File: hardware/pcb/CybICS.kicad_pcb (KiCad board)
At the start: 2 copper layers, 160 x 100 mm, 79 parts, among them J1 Raspberry_Pi_2_3, J2 Conn_01x03_Pin, J3 Conn_01x05_Pin, J4 USB_C_Receptacle_USB2.0, SW1 SW_Push, SW2 SW_Push, SW3 SW_Push, U1 STM32G070RBTx

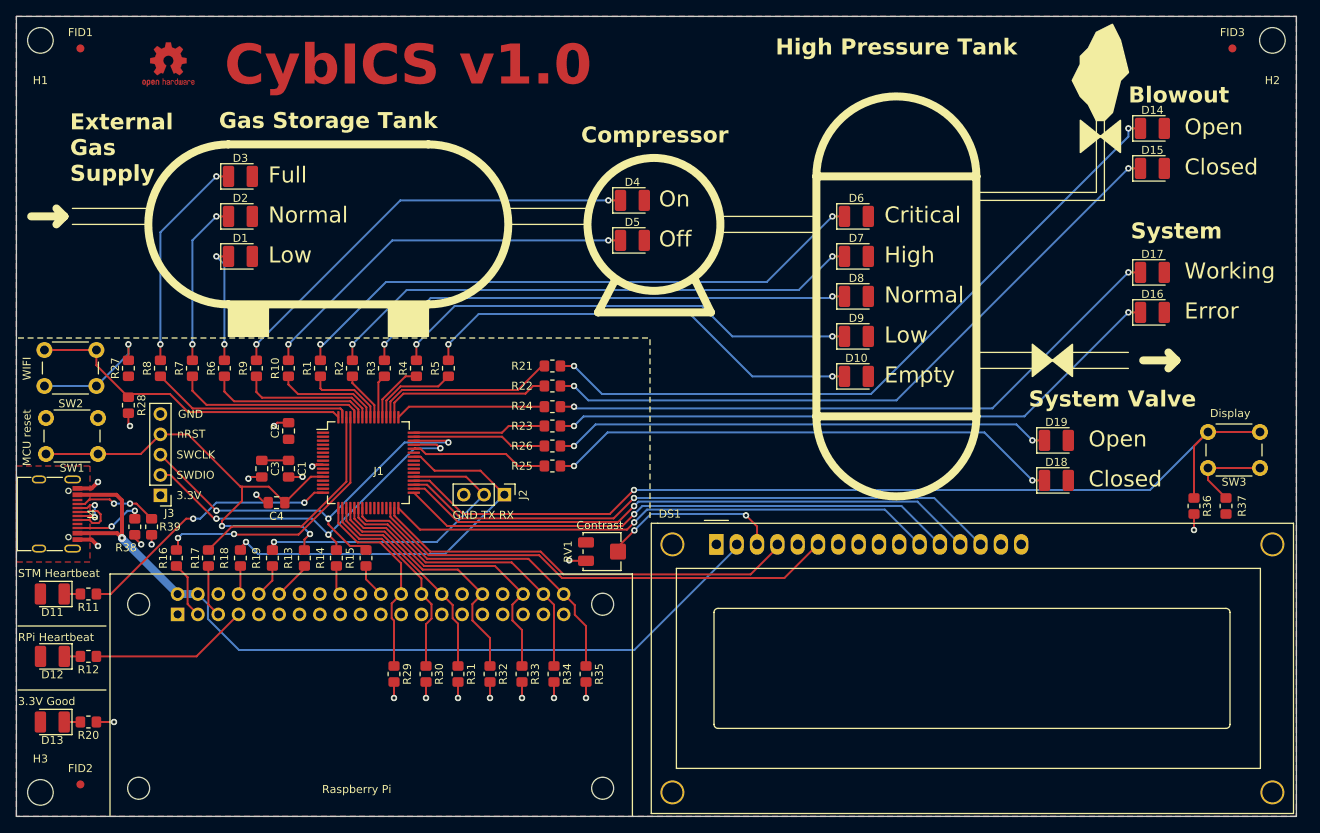
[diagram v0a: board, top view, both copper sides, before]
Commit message: feat(hardware)!: hardware v1.1 upgrade, KiCad 10 and JLCPCB fixes (#240)
* fix(hardware): exclude fiducials from the JLCPCB position files

FID1-FID3 carried exclude_from_bom but not exclude_from_pos_files,
unlike the mounting holes and the OSHW logo, which set both. The
fiducials therefore reached the CPL while being absent from the BOM,
and JLCPCB rejected the assembly quote with "FID1,FID2,FID3
designators don't exist in the BOM file" (reported in #238). Fiducials
are alignment marks rather than parts, so the dialog was harmless, but
every person ordering this board had to decide that for themselves.

Verified with kicad-cli 8.0.9: pcb export pos --smd-only drops from 69
to 66 rows against the previous board, the three removed designators
are exactly FID1, FID2 and FID3, and ERC and DRC still report 0
violations and 0 unconnected items. Claude has no access to the
hardware, so the JLCPCB upload itself is unverified.

Refs #238

Co-Authored-By: Claude Opus 5 (1M context) <noreply@anthropic.com>
Claude-Session: https://claude.ai/code/session_011zbigHZaGiZii3etPu8DwT

* fix(hardware): correct the LED series resistors and the yellow LED part

R1/R2/R4/R6/R10/R21/R23/R25 are drawn as 330R but carried C52548, which
is 0805W8F330LT5E -- 330 mΩ, not 330 Ω. The L in that part code is
Uniroyal's milliohm marker, and both LCSC and JLCPCB's parts database
index it at 0.33 Ω. The six red, two yellow and two blue indicators
were therefore assembled with no effective current limiting: each one
settles at roughly its full rated current against the GPIO's own
impedance, and ten such pins take the STM32G070 past its 100 mA total
I/O budget. Corrected to C17630 (0805W8F3300T5E, 330 Ω), which is also
a basic-library part.

That correction alone would have regressed two colours, because the
0.33 Ω part was the only reason they lit at all:

  - D7/D9 are drawn as LED YELLOW but carried C434441, SZYY1206W -- a
    *white* LED with a yellow lens and Vf 3.1 V. Across a real 330 Ω
    fro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
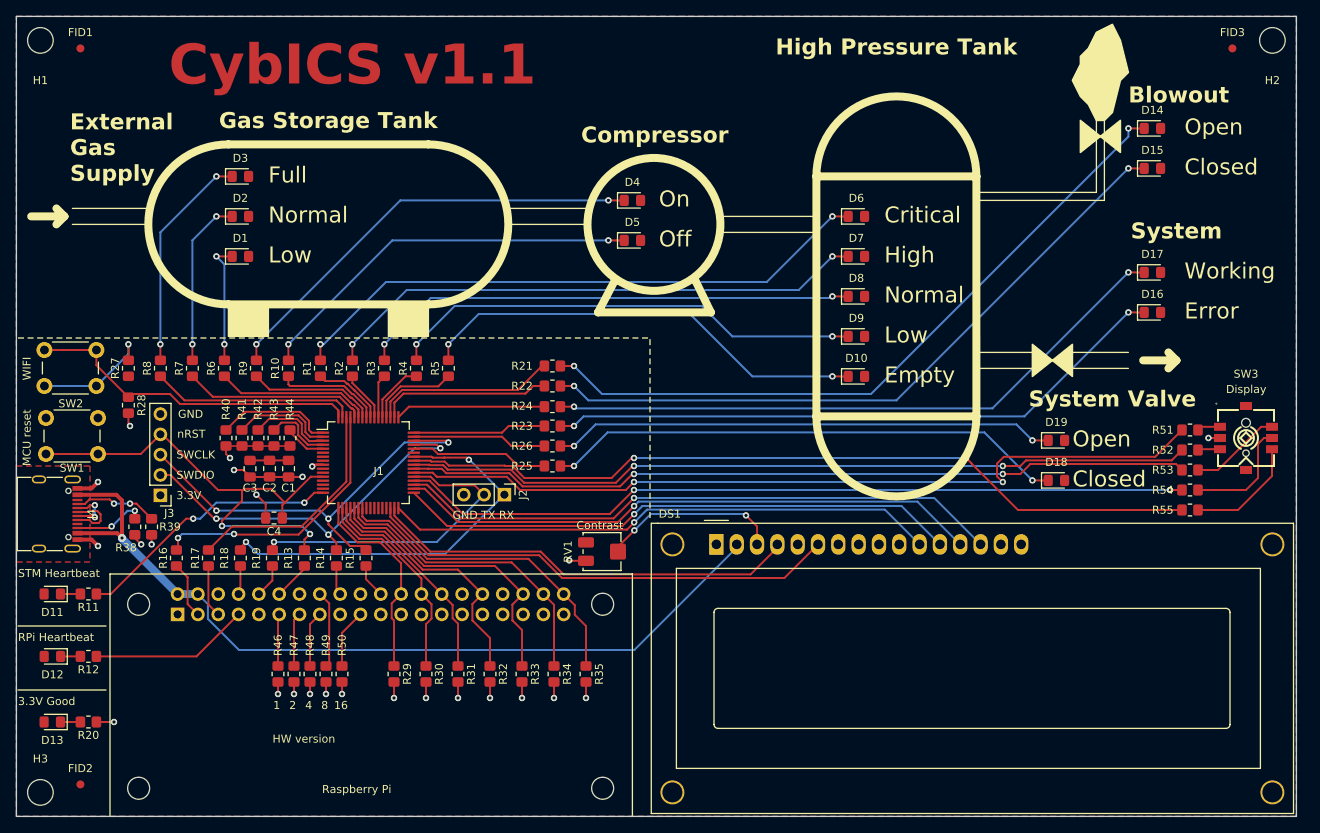
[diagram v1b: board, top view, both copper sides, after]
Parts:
- removed #SYM1: OSHW-Logo2_7.3x6mm_Copper, Symbol:OSHW-Logo2_7.3x6mm_Copper
- removed R36: 10kR, Resistor_SMD:R_0805_2012Metric_Pad1.20x1.40mm_HandSolder
- removed R37: 1kR, Resistor_SMD:R_0805_2012Metric_Pad1.20x1.40mm_HandSolder
- added R40: 1kR, Resistor_SMD:R_0805_2012Metric_Pad1.20x1.40mm_HandSolder, F.Cu at (77.0, 103.5)
- added R41: 1kR, Resistor_SMD:R_0805_2012Metric_Pad1.20x1.40mm_HandSolder, F.Cu at (79.0, 103.5)
- added R42: 1kR, Resistor_SMD:R_0805_2012Metric_Pad1.20x1.40mm_HandSolder, F.Cu at (81.0, 103.5)
- added R43: 1kR, Resistor_SMD:R_0805_2012Metric_Pad1.20x1.40mm_HandSolder, F.Cu at (83.0, 103.5)
- added R44: 1kR, Resistor_SMD:R_0805_2012Metric_Pad1.20x1.40mm_HandSolder, F.Cu at (85.0, 103.5)
- added R46: 1kR, Resistor_SMD:R_0805_2012Metric_Pad1.20x1.40mm_HandSolder, F.Cu at (83.5, 133.0)
- added R47: 1kR, Resistor_SMD:R_0805_2012Metric_Pad1.20x1.40mm_HandSolder, F.Cu at (85.5, 133.0)
- added R48: 1kR, Resistor_SMD:R_0805_2012Metric_Pad1.20x1.40mm_HandSolder, F.Cu at (87.5, 133.0)
- added R49: 1kR, Resistor_SMD:R_0805_2012Metric_Pad1.20x1.40mm_HandSolder, F.Cu at (89.5, 133.0)
- added R50: 1kR, Resistor_SMD:R_0805_2012Metric_Pad1.20x1.40mm_HandSolder, F.Cu at (91.5, 133.0)
- added R51: 1kR, Resistor_SMD:R_0805_2012Metric_Pad1.20x1.40mm_HandSolder, F.Cu at (197.5, 102.5)
- added R52: 1kR, Resistor_SMD:R_0805_2012Metric_Pad1.20x1.40mm_HandSolder, F.Cu at (197.5, 105.0)
- added R53: 1kR, Resistor_SMD:R_0805_2012Metric_Pad1.20x1.40mm_HandSolder, F.Cu at (197.5, 107.5)
- added R54: 1kR, Resistor_SMD:R_0805_2012Metric_Pad1.20x1.40mm_HandSolder, F.Cu at (197.5, 110.0)
- added R55: 1kR, Resistor_SMD:R_0805_2012Metric_Pad1.20x1.40mm_HandSolder, F.Cu at (197.5, 112.5)
- D1, D11, D12, D13, D14, D15, D16, D17, D18, D19, D2, D4, D5, D6, D7, D8, D9: footprint LED_SMD:LED_1210_3225Metric_Pad1.42x2.65mm_HandSolder -> LED_SMD:LED_0805_2012Metric_Pad1.15x1.40mm_HandSolder
- D10, D3: value LED BLUE -> LED WHITE; footprint LED_SMD:LED_1210_3225Metric_Pad1.42x2.65mm_HandSolder -> LED_SMD:LED_0805_2012Metric_Pad1.15x1.40mm_HandSolder
- R11, R12, R20, R22, R24, R26, R3, R7, R9: value 100R -> 1kR
- R5, R8: value 330R -> 100R
- SW3: value SW_Push -> 7*7*5-6P-L WX; footprint Button_Switch_THT:SW_PUSH_6mm_H5mm -> cybics:SW-SMD_8P-L7.0-W7.0-P1.40-LS7.4-TL
- moved C2 5.27 mm to (82.4, 107.3), turned to -90 degrees
- moved SW3 4.81 mm to (204.5, 103.5)
- moved C4 1.94 mm to (83.0, 113.5)
- moved C3 1.47 mm to (80.0, 107.3)
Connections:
- J1 pad 11: unconnected-(J1-GPIO17-Pad11) -> /HWV_RPI0
- J1 pad 13: unconnected-(J1-GPIO27-Pad13) -> /HWV_RPI1
- J1 pad 15: unconnected-(J1-GPIO22-Pad15) -> /HWV_RPI2
- J1 pad 16: unconnected-(J1-GPIO23-Pad16) -> /HWV_RPI3
- J1 pad 19: unconnected-(J1-MOSI0/GPIO10-Pad19) -> /HWV_RPI4
- SW3 pad 1: /PA8 -> Net-(SW3-F2)
- SW3 pad 2: Net-(R37-Pad2) -> GND
- U1 pad 1: unconnected-(U1-PC11-Pad1) -> /HWV_STM0
- U1 pad 2: unconnected-(U1-PC12-Pad2) -> /HWV_STM1
- U1 pad 3: unconnected-(U1-PC13-Pad3) -> /HWV_STM2
- U1 pad 38: unconnected-(U1-PC6-Pad38) -> /NAV_F2
- U1 pad 39: unconnected-(U1-PC7-Pad39) -> /NAV_F3
- U1 pad 4: unconnected-(U1-PC14-Pad4) -> /HWV_STM3
- U1 pad 40: unconnected-(U1-PD8-Pad40) -> /NAV_F4
- U1 pad 41: unconnected-(U1-PD9-Pad41) -> /NAV_F5
- U1 pad 5: unconnected-(U1-PC15-Pad5) -> /HWV_STM4
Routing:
- net /NAV_F2: track 0.00 -> 102.4 mm, vias 0 -> 2
- net /NAV_F5: track 0.00 -> 100.7 mm, vias 0 -> 2
- net /NAV_F4: track 0.00 -> 98.7 mm, vias 0 -> 2
- net /NAV_F3: track 0.00 -> 98.4 mm, vias 0 -> 2
- net /PA8: track 120.7 -> 99.0 mm, vias 1 -> 2
- net /HWV_STM0: track 0.00 -> 14.8 mm
- net Net-(SW3-F1): track 0.00 -> 14.4 mm
- net Net-(SW3-F5): track 0.00 -> 14.4 mm
- net GND: track 40.3 -> 53.9 mm, vias 20 -> 25
- net /HWV_STM1: track 0.00 -> 12.7 mm
- net Net-(SW3-F3): track 0.00 -> 11.5 mm
- net Net-(R37-Pad2): track 11.2 -> 0.00 mm
- net /HWV_STM2: track 0.00 -> 10.6 mm
- net /HWV_RPI3: track 0.00 -> 9.64 mm
- net /HWV_STM3: track 0.00 -> 8.37 mm
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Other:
- board text added: "1"
- board text added: "16"
- board text added: "2"
- board text added: "4"
- board text added: "8"
- board text added: "CybICS v1.1"
- board text added: "HW version"
- board text removed: "CybICS v1.0"

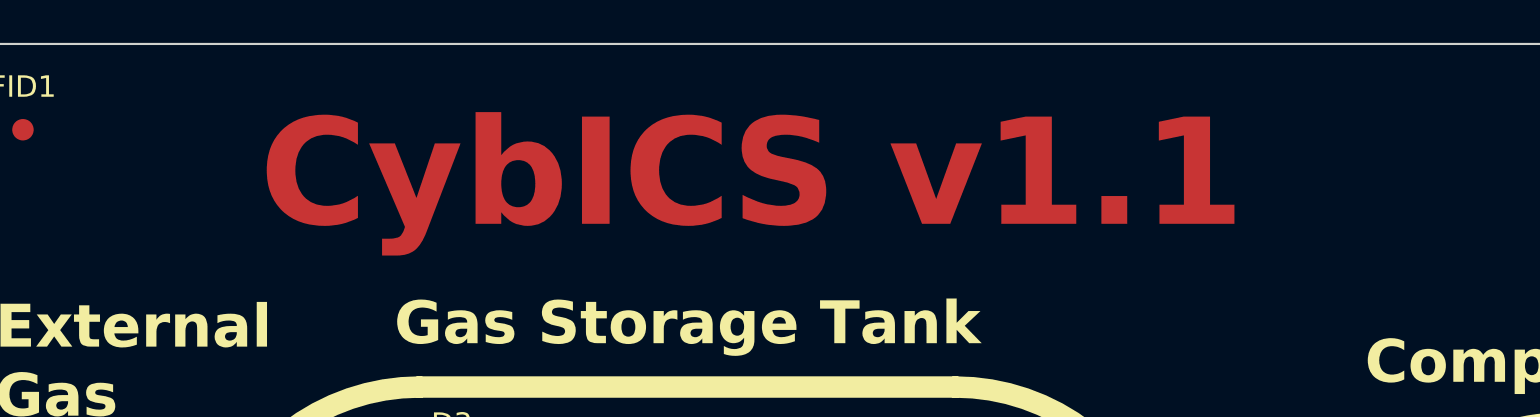
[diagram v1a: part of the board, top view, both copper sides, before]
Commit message: fix(hardware): restore the open hardware logo and make room for it
The OSHW logo on `F.Cu` disappeared from the board somewhere inside #240 and
nobody noticed until after the merge.

**How it was lost.** It went in `bada93a`, a commit whose message describes only
the navigation switch's non-plated holes but whose board diff is 9992 lines
because it absorbed a relayout done in the GUI. The mechanism is not a slip of
the mouse: the schematic symbol `#SYM1` (`Graphic:Logo_Open_Hardware_Small`)
carries `(on_board no)`, so *Update PCB from Schematic* with **Delete footprints
with no symbols** removes its placed footprint. `FID1`-`FID3` and `H1`-`H3` have
symbols with `on_board yes`, which is why they survived the same operation.

**How it is prevented from happening again.** The footprint is placed with
`(attr board_only ...)`, which is exactly what that attribute is for: KiCad does
not delete board-only footprints when updating from the schematic. Marking it
also settled a question the first attempt got wrong -- linking the footprint to
the symbol by `path` instead made the parity check report `extra_footprint`,
because a `#`-prefixed reference is a virtual symbol that never belongs on the
board. `board_only` gives 0 parity issues.

**It needs its soldermask apertures.** `Symbol:OSHW-Logo2_7.3x6mm_Copper` from
the KiCad library is copper only, and copper under mask renders as dark green.
The footprint that was on the board carried 13 `F.Mask` polygons alongside its
13 on `F.Cu`, so the logo showed as bare gold like the board title. Those 13 are
restored, counted against the original rather than eyeballed.

**It no longer fits where it was.** `35c885b` re-centred the title in its copper
window, and that is what squeezed the logo out visually rather than
electrically. Measured with `GetBoundingBox`: the window is 62.80..122.80 mm,
"CybICS v1.1" spans 69.30..116.30, so each side has a 6.50 mm gap and the logo
is 6.53 mm wide. It misses by 0.03 mm. Restoring it at the old 6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
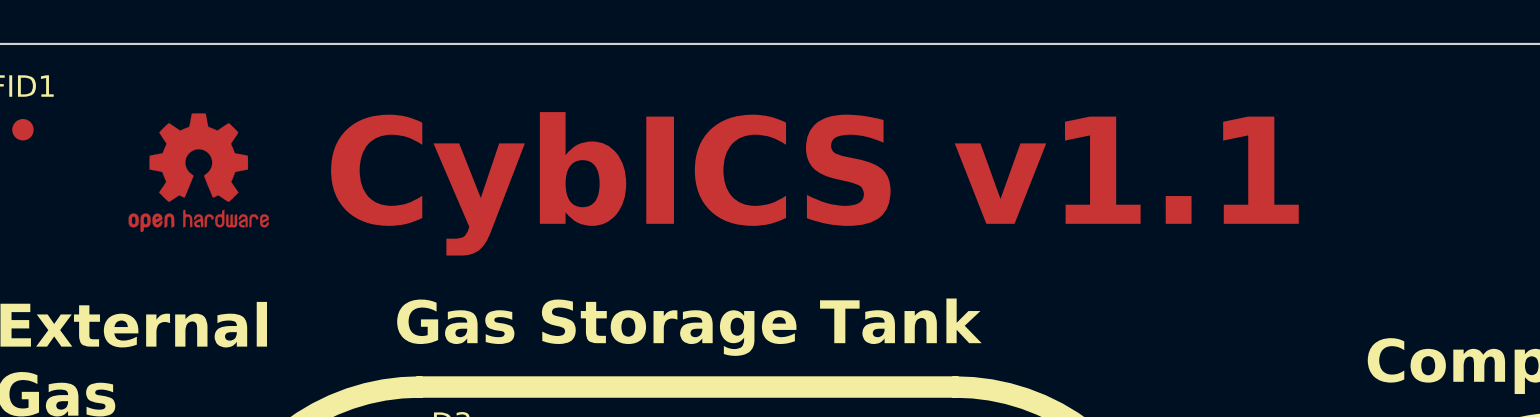
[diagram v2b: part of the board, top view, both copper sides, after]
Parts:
- added #SYM1: OSHW-Logo2_7.3x6mm_Copper, Symbol:OSHW-Logo2_7.3x6mm_Copper, F.Cu at (67.0, 56.8)

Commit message: fix(hardware): keep the logo in the project library so a library update keeps it
`board_only` stops `Update PCB from Schematic` deleting the logo, but it does
nothing against `Tools > Update Footprints from Library`, which is a separate
operation that re-reads the footprint from its library and replaces the placed
graphics. `Symbol:OSHW-Logo2_7.3x6mm_Copper` as KiCad ships it has **zero**
`F.Mask` polygons and no `board_only` in its `attr` line, so one library update
would have put the logo back under soldermask -- dark green on dark green -- and
dropped the flag protecting it from the next F8. The restore would have survived
exactly until someone ran the other update.

The footprint therefore moves into `cybics.pretty`, the project library that
already carries the navigation switch, with the 13 `F.Mask` apertures and
`board_only` baked in, and the board references
`cybics:OSHW-Logo2_7.3x6mm_Copper`.

Verified that a library update is now a no-op for it: loading the placed
footprint and the project library footprint through `pcbnew` and comparing their
graphics position-normalised gives 26 shapes each, 13 on `F.Cu` and 13 on
`F.Mask`, with identical geometry, and both report `FP_BOARD_ONLY`. DRC with
`--refill-zones --schematic-parity` still reports 0 violations, 0 unconnected
items and 0 parity issues, and the render is unchanged.

CLAUDE.md gains the rule this came from: a board-only footprint that differs
from its stock library version belongs in `cybics.pretty`, or the difference is
one menu item from being erased.

Co-Authored-By: Claude Opus 5 (1M context) <noreply@anthropic.com>
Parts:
- #SYM1: footprint Symbol:OSHW-Logo2_7.3x6mm_Copper -> cybics:OSHW-Logo2_7.3x6mm_Copper
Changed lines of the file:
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@@
 		)
 	)
-	(footprint "Symbol:OSHW-Logo2_7.3x6mm_Copper"
+	(footprint "cybics:OSHW-Logo2_7.3x6mm_Copper"
 		(layer "F.Cu")
 		(at 67 56.8)

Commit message: fix: balance the LED brightness on v1.1 boards (#274)
* fix(hardware): fit 20k to the three status LEDs on v1.1

The three greens on the left edge -- D11 (STM32 heartbeat), D12
(Raspberry Pi heartbeat) and D13 (power) -- sit on 1k, and v1.1's green,
C2297, is efficient enough that they glare at that current. D13 is tied
straight to 3V3 and cannot be dimmed from either controller at all. On a
board reworked to 20k for R11, R12 and R20 the brightness was judged
acceptable by eye, so the v1.1 BOM now fits that value: UNI-ROYAL
0805W8F2002T5E, JLCPCB Basic part C4328, the same 0805 family as the
C17513 1k it replaces.

Only the Value and JLCPCB Part # fields of R11, R12 and R20 change, in
the schematic and on the board; footprints, nets and layout are
untouched.

Verified with setsoft/kicad_auto:ki10 (KiCad 10): ERC with errors as
failures exits 0, DRC with --schematic-parity reports 0 violations and 0
unconnected pads, and the exported BOM groups "R11,R12,R20 / 20kR /
C4328". The generated docs under hardware/pcb/docs are left to
kibotVerify.yml.

Co-Authored-By: Claude Opus 5.5 <noreply@anthropic.com>

* fix(stm32): dim the process LEDs per board revision

The output thread has always run every LED except the greens at about
one fifteenth duty and left the greens fully on. That suited v1.0, whose
green part was much dimmer than its red, yellow and blue. v1.1 moved all
LEDs to JLCPCB Basic parts, and its green (C2297) is an order of
magnitude more efficient: on a v1.1 board the greens glare while red,
yellow and white look faint.

Brightness is now a table per board revision and per colour, chosen at
start-up from the version straps. The v1.0 table reproduces the old
behaviour exactly; v1.1 and unknown newer boards get green 10 %, red
40 %, yellow 50 % and white 15 %, the shares tuned by eye on a v1.1 board
on the earlier fix/green-led-brightness branch. The PWM runs at 100 Hz
and wakes once per colour per period, using the 10 kHz kernel tick for
1 % resolution.

The t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
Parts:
- R11, R12, R20: value 1kR -> 20kR
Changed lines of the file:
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@@
 			)
 		)
-		(property "Value" "1kR"
+		(property "Value" "20kR"
 			(at 0 1.65 0)
 			(layer "F.Fab")
@@
 			)
 		)
-		(property "JLCPCB Part #" "C17513"
+		(property "JLCPCB Part #" "C4328"
 			(at 119.6 246 0)
 			(layer "F.Fab")
@@
 			)
 		)
-		(property "Value" "1kR"
+		(property "Value" "20kR"
 			(at 0 1.65 0)
 			(layer "F.Fab")
@@
 			)
 		)
-		(property "JLCPCB Part #" "C17513"
+		(property "JLCPCB Part #" "C4328"
 			(at 119.6 261.6 0)
 			(layer "F.Fab")
@@
 			)
 		)
-		(property "Value" "1kR"
+		(property "Value" "20kR"
 			(at 0 1.65 0)
 			(layer "F.Fab")
@@
 			)
 		)
-		(property "JLCPCB Part #" "C17513"
+		(property "JLCPCB Part #" "C4328"
 			(at 119.6 278 0)
 			(layer "F.Fab")
